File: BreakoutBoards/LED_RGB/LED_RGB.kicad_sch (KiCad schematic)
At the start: 6 parts, among them J1 Conn_01x04_Pin

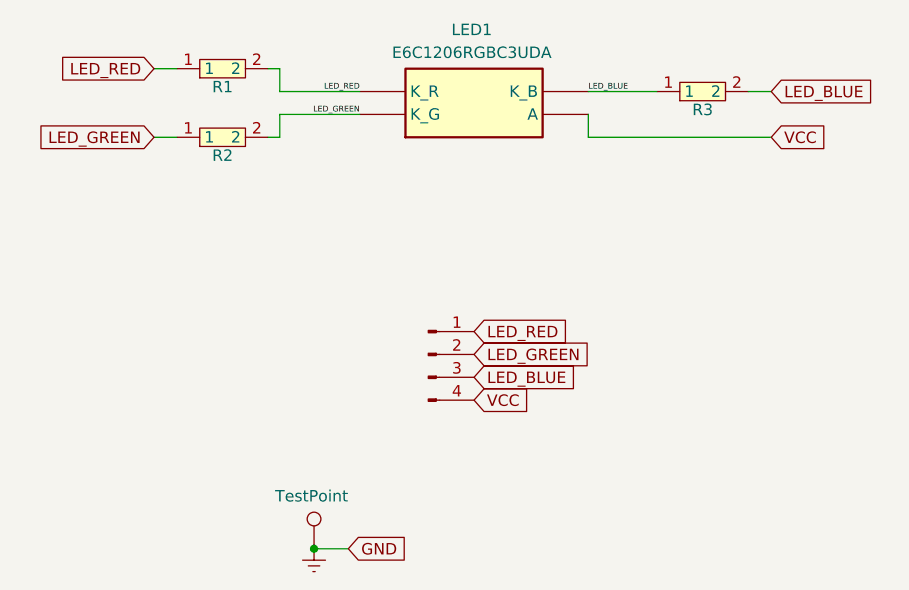
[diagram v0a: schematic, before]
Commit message: tweaked silkscreen positions
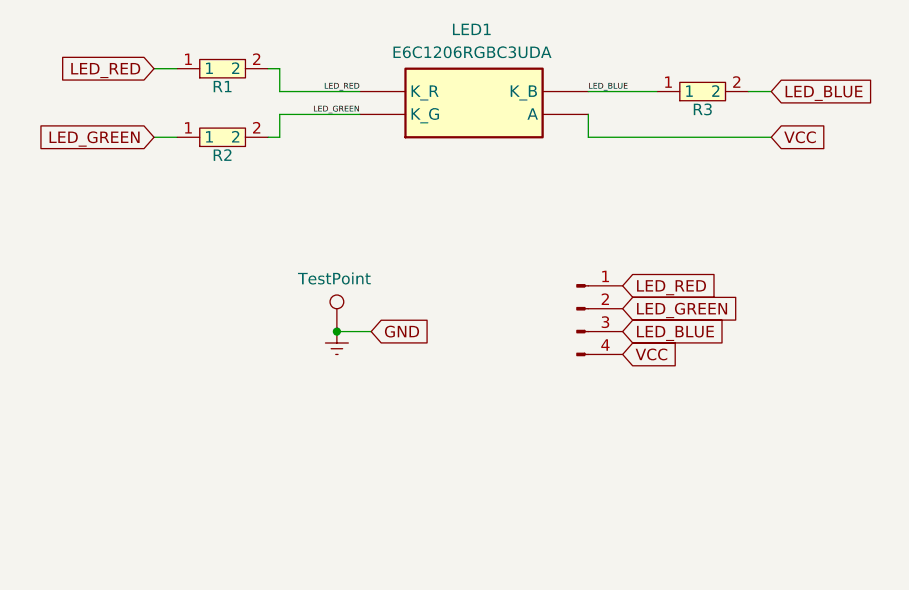
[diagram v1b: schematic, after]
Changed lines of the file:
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@@
 	)
 	(junction
-		(at 80.01 135.89)
+		(at 82.55 111.76)
 		(diameter 0)
 		(color 0 0 0 0)
@@
 	(wire
 		(pts
-			(xy 83.82 135.89) (xy 80.01 135.89)
+			(xy 86.36 111.76) (xy 82.55 111.76)
 		)
 		(stroke
@@
 	(global_label "VCC"
 		(shape input)
-		(at 97.79 119.38 0)
+		(at 114.3 114.3 0)
 		(fields_autoplaced yes)
 		(effects
@@
 		)
 		(property "Intersheetrefs" "${INTERSHEET_REFS}"
-			(at 104.4038 119.38 0)
+			(at 120.9138 114.3 0)
 			(effects
 				(font
@@
 	(global_label "GND"
 		(shape input)
-		(at 83.82 135.89 0)
+		(at 86.36 111.76 0)
 		(fields_autoplaced yes)
 		(effects
@@
 		)
 		(property "Intersheetrefs" "${INTERSHEET_REFS}"
-			(at 90.6757 135.89 0)
+			(at 93.2157 111.76 0)
 			(effects
 				(font
@@
 	(global_label "LED_BLUE"
 		(shape input)
-		(at 97.79 116.84 0)
+		(at 114.3 111.76 0)
 		(fields_autoplaced yes)
 		(effects
@@
 		)
 		(property "Intersheetrefs" "${INTERSHEET_REFS}"
-			(at 109.9675 116.84 0)
+			(at 126.4775 111.76 0)
 			(effects
 				(font
@@
 	(global_label "LED_RED"
 		(shape input)
-		(at 97.79 111.76 0)
+		(at 114.3 106.68 0)
 		(fields_autoplaced yes)
 		(effects
@@
 		)
 		(property "Intersheetrefs" "${INTERSHEET_REFS}"
-			(at 108.8789 111.76 0)
+			(at 125.3889 106.68 0)
 			(effects
 				(font
@@
 	(global_label "LED_GREEN"
 		(shape input)
-		(at 97.79 114.3 0)
+		(at 114.3 109.22 0)
 		(fields_autoplaced yes)
 		(effects
@@
 		)
 		(property "Intersheetrefs" "${INTERSHEET_REFS}"
-			(at 111.3584 114.3 0)
+			(at 127.8684 109.22 0)
 			(effects
 				(font
@@
 	(symbol
 		(lib_id "power:GNDREF")
-		(at 80.01 135.89 0)
+		(at 82.55 111.76 0)
 		(unit 1)
 		(exclude_from_sim no)
@@
 		(fields_autoplaced yes)
 		(property "Reference" "#PWR01"
-			(at 80.01 142.24 0)
+			(at 82.55 118.11 0)
 			(effects
 				(font
@@
 		)
 		(property "Value" "GND"
-			(at 80.01 140.97 0)
+			(at 82.55 116.84 0)
 			(effects
 				(font
@@
 		)
 		(property "Footprint" ""
-			(at 80.01 135.89 0)
+			(at 82.55 111.76 0)
 			(effects
 				(font
@@
 		)
 		(property "Datasheet" ""
-			(at 80.01 135.89 0)
+			(at 82.55 111.76 0)
 			(effects
 				(font
@@
 		)
 		(property "Description" "Power symbol creates a global label with name \"GNDREF\" , reference supply ground"
-			(at 80.01 135.89 0)
+			(at 82.55 111.76 0)
 			(effects
 				(font
@@
 	(symbol
 		(lib_id "Connector:Conn_01x04_Pin")
-		(at 92.71 114.3 0)
+		(at 109.22 109.22 0)
 		(unit 1)
 		(exclude_from_sim no)
@@
 		(fields_autoplaced yes)
 		(property "Reference" "J1"
-			(at 93.345 109.22 0)
+			(at 109.855 104.14 0)
 			(effects
 				(font
@@
 		)
 		(property "Value" "Conn_01x04_Pin"
-			(at 93.345 109.22 0)
+			(at 109.855 104.14 0)
 			(effects
 				(font
@@
 		)
 		(property "Footprint" "clectric-diy:HDR-TH_4P-P2.54-V-M"
-			(at 92.71 114.3 0)
+			(at 109.22 109.22 0)
 			(effects
 				(font
@@
 		)
 		(property "Datasheet" "~"
-			(at 92.71 114.3 0)
+			(at 109.22 109.22 0)
 			(effects
 				(font
@@
 		)
 		(property "Description" "Generic connector, single row, 01x04, script generated"
-			(at 92.71 114.3 0)
+			(at 109.22 109.22 0)
 			(effects
 				(font
@@
 	(symbol
 		(lib_id "Connector:TestPoint")
-		(at 80.01 135.89 0)
+		(at 82.55 111.76 0)
 		(unit 1)
 		(exclude_from_sim no)
@@
 		(dnp no)
 		(property "Reference" "TP1"
-			(at 82.55 131.3179 0)
+			(at 85.09 107.1879 0)
 			(effects
 				(font
@@
 		)
 		(property "Value" "TestPoint"
-			(at 75.692 130.048 0)
+			(at 78.232 105.918 0)
 			(effects
 				(font
@@
 		)
 		(property "Footprint" "TestPoint:TestPoint_THTPad_D1.0mm_Drill0.5mm"
-			(at 85.09 135.89 0)
+			(at 87.63 111.76 0)
 			(effects
 				(font
@@
 		)
 		(property "Datasheet" "~"
-			(at 85.09 135.89 0)
+			(at 87.63 111.76 0)
 			(effects
 				(font
@@
 		)
 		(property "Description" "test point"
-			(at 80.01 135.89 0)
-			(effects
-				(font
+			(at 82.55 111.76 0)
+			(effects
+				(font
